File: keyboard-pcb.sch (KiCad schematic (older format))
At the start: 14 parts

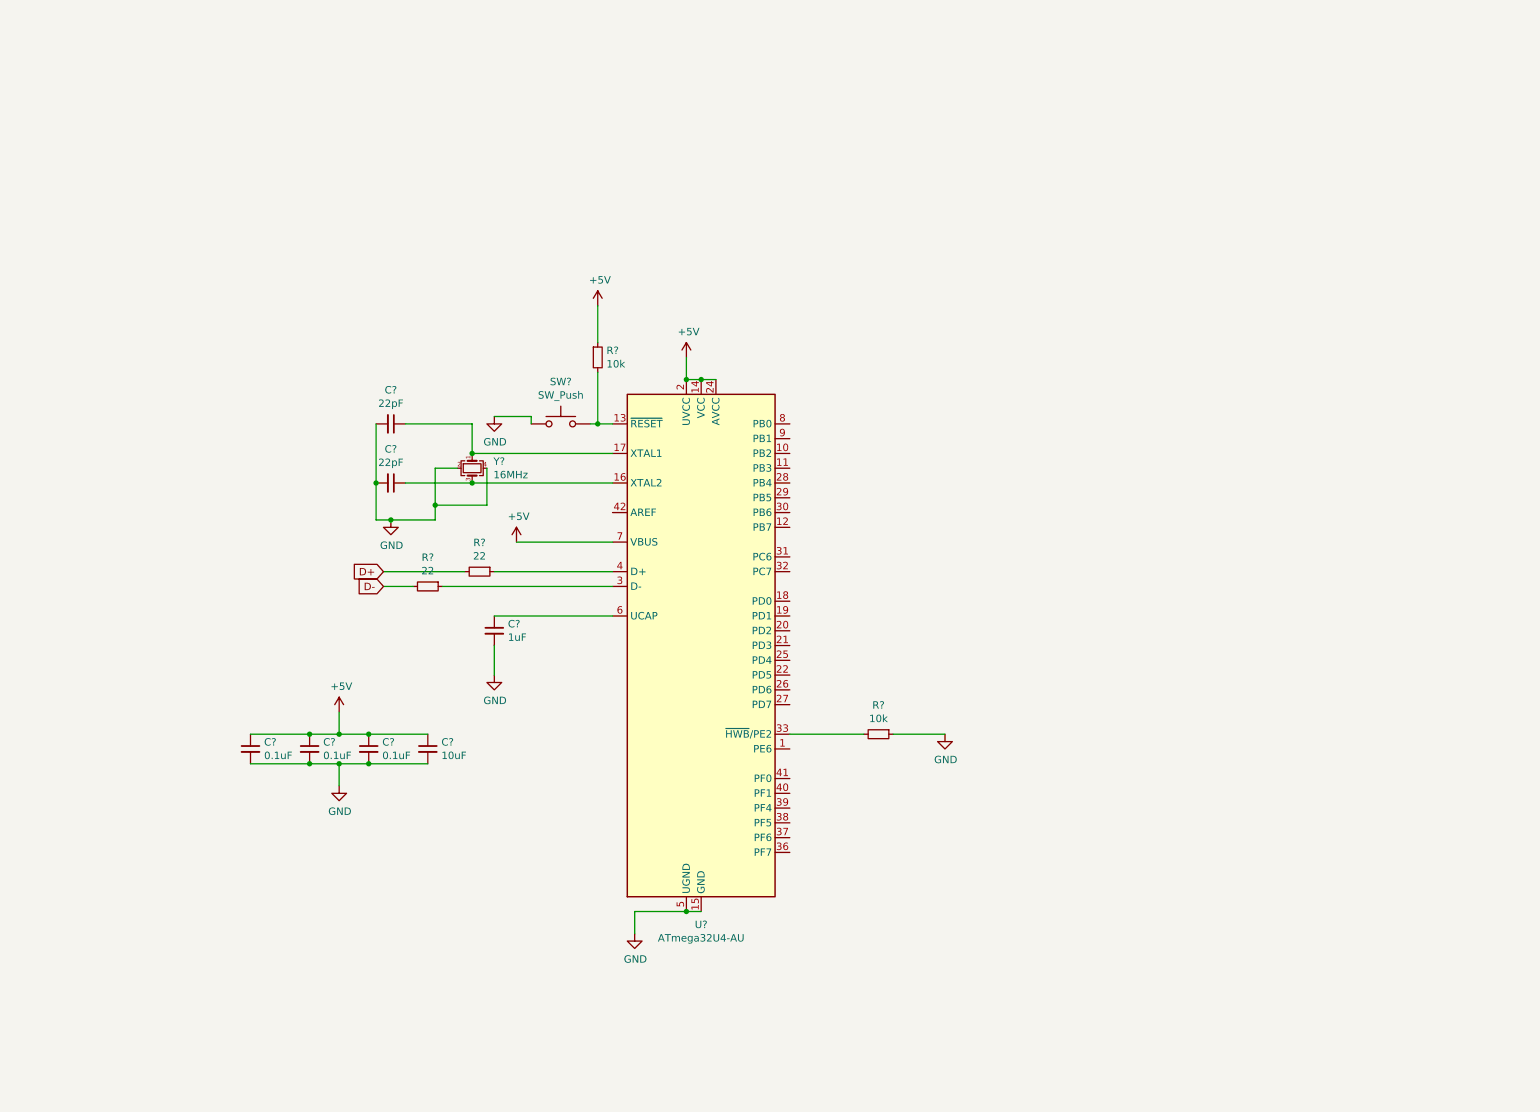
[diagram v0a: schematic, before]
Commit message: Completed Switch Matrix
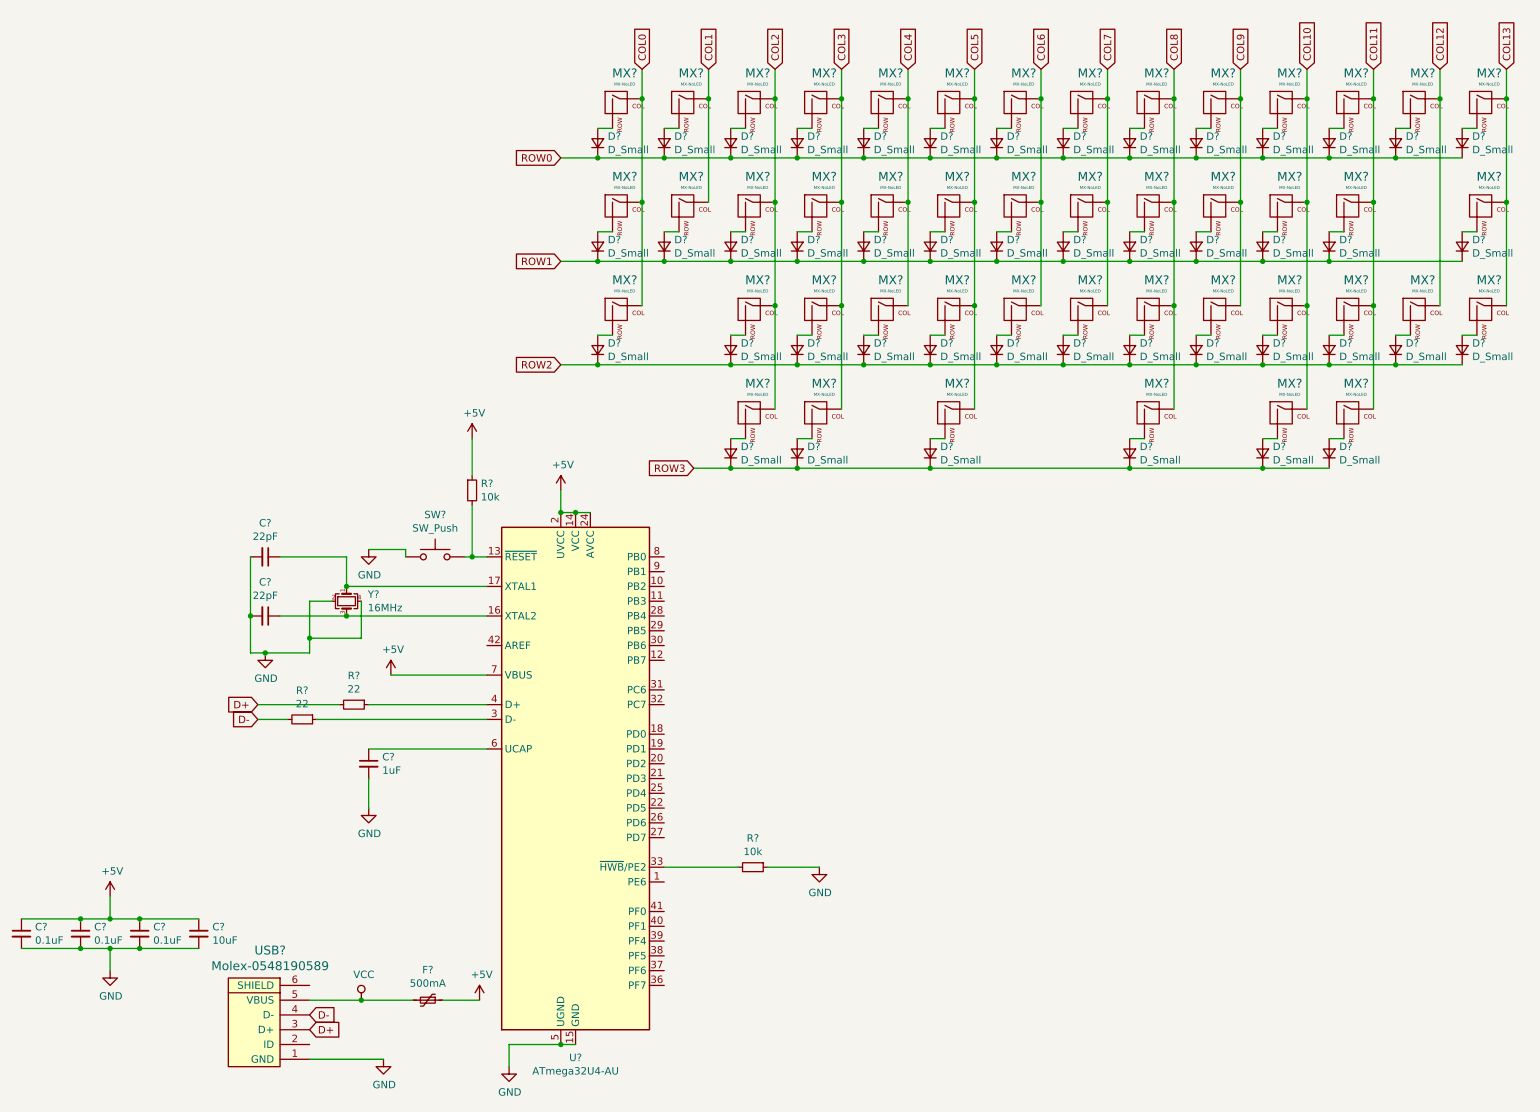
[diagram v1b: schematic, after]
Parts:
- added D? (x46): D_Small, symbol Device:D_Small
- added F?: 500mA, symbol Device:Polyfuse_Small
- added MX? (x46): MX-NoLED, symbol MX_Alps_Hybrid:MX-NoLED
- added USB?: Molex-0548190589, symbol random-keyboard-parts:Molex-0548190589
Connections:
- net +5V: now also F?.1
- net D+: now also USB?.3 (D+)
- net D-: now also USB?.4 (D-)
- net GND: now also USB?.1 (GND)
- new net: D?.2 (A), MX?.2 (ROW) (x46)
- new net COL0: MX?.1 (COL), MX?.1 (COL), MX?.1 (COL)
- new net COL1: MX?.1 (COL), MX?.1 (COL)
- new net COL10: MX?.1 (COL), MX?.1 (COL), MX?.1 (COL), MX?.1 (COL)
- new net COL11: MX?.1 (COL), MX?.1 (COL), MX?.1 (COL), MX?.1 (COL)
- new net COL12: MX?.1 (COL), MX?.1 (COL)
- new net COL13: MX?.1 (COL), MX?.1 (COL), MX?.1 (COL)
- new net COL2: MX?.1 (COL), MX?.1 (COL), MX?.1 (COL), MX?.1 (COL)
- new net COL3: MX?.1 (COL), MX?.1 (COL), MX?.1 (COL), MX?.1 (COL)
- new net COL4: MX?.1 (COL), MX?.1 (COL), MX?.1 (COL)
- new net COL5: MX?.1 (COL), MX?.1 (COL), MX?.1 (COL), MX?.1 (COL)
- new net COL6: MX?.1 (COL), MX?.1 (COL), MX?.1 (COL)
- new net COL7: MX?.1 (COL), MX?.1 (COL), MX?.1 (COL)
- new net COL8: MX?.1 (COL), MX?.1 (COL), MX?.1 (COL), MX?.1 (COL)
- new net COL9: MX?.1 (COL), MX?.1 (COL), MX?.1 (COL)
- new net ROW0: D?.1 (K), D?.1 (K), D?.1 (K), D?.1 (K), D?.1 (K), D?.1 (K), D?.1 (K), D?.1 (K), D?.1 (K), D?.1 (K), D?.1 (K), D?.1 (K), D?.1 (K), D?.1 (K)
- new net ROW1: D?.1 (K), D?.1 (K), D?.1 (K), D?.1 (K), D?.1 (K), D?.1 (K), D?.1 (K), D?.1 (K), D?.1 (K), D?.1 (K), D?.1 (K), D?.1 (K), D?.1 (K)
- new net ROW2: D?.1 (K), D?.1 (K), D?.1 (K), D?.1 (K), D?.1 (K), D?.1 (K), D?.1 (K), D?.1 (K), D?.1 (K), D?.1 (K), D?.1 (K), D?.1 (K), D?.1 (K)
- new net ROW3: D?.1 (K), D?.1 (K), D?.1 (K), D?.1 (K), D?.1 (K), D?.1 (K)
- new net VCC: F?.2, USB?.5 (VBUS)
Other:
- moved on the sheet: C?, R?, SW?, U?, Y?
